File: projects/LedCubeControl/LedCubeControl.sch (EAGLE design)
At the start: 30 parts, among them IC1 74HC595N, IC2 74HC595N, IC3 74HC595N, T1 PN2222A, T2 PN2222A, T3 PN2222A, T4 PN2222A

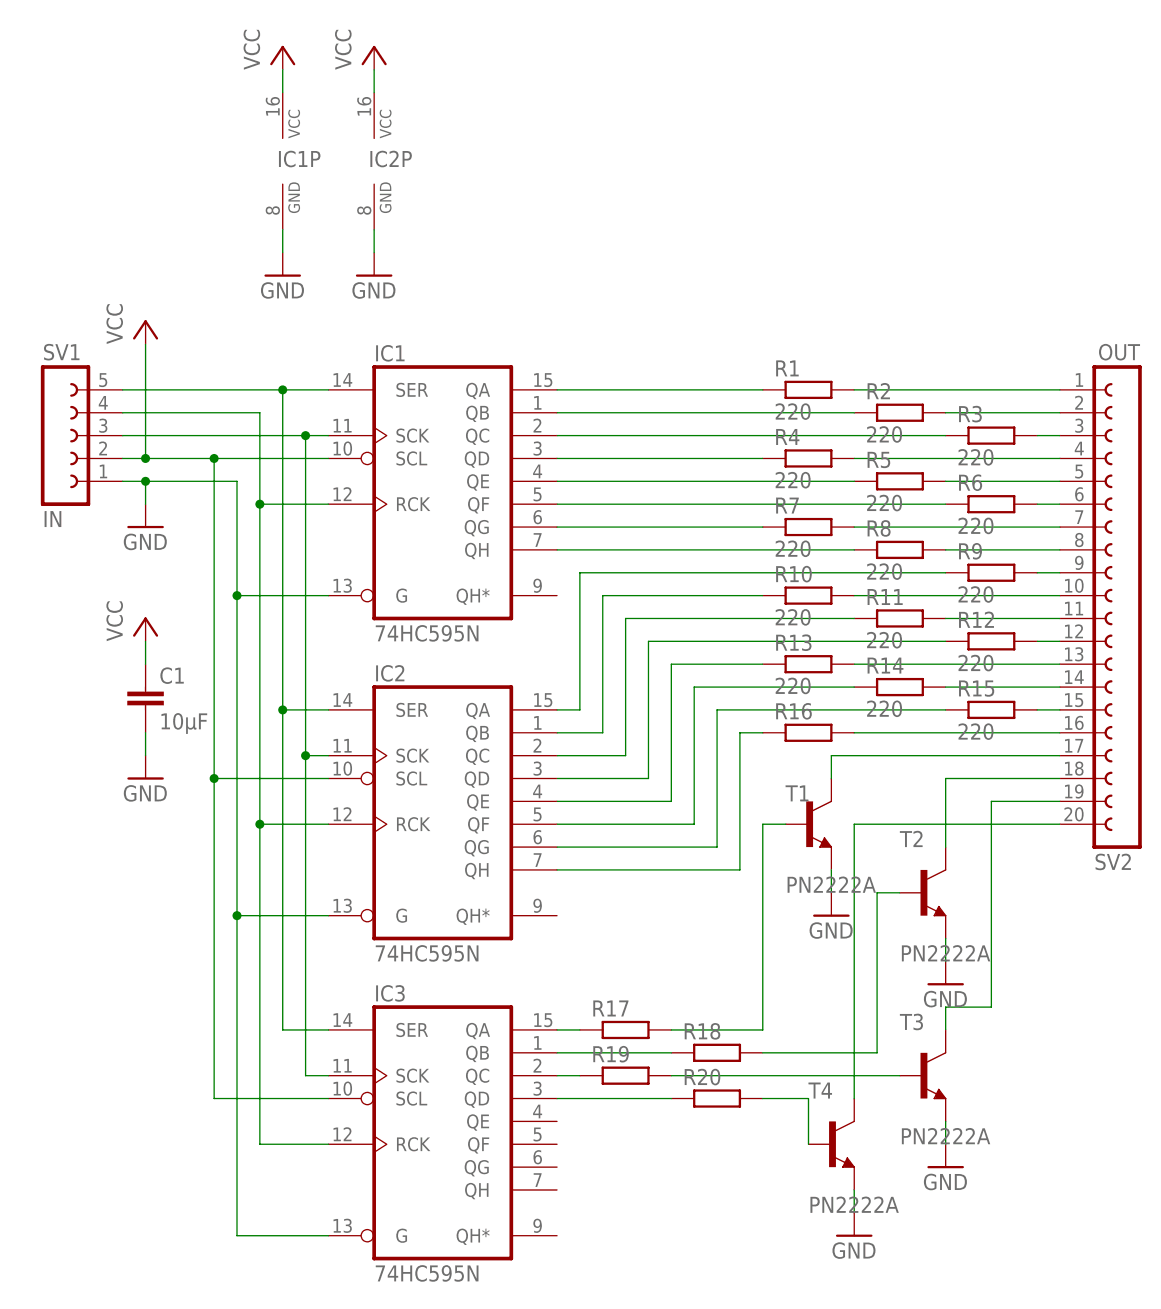
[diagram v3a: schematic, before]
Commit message: fix: mwrt and led control fixed
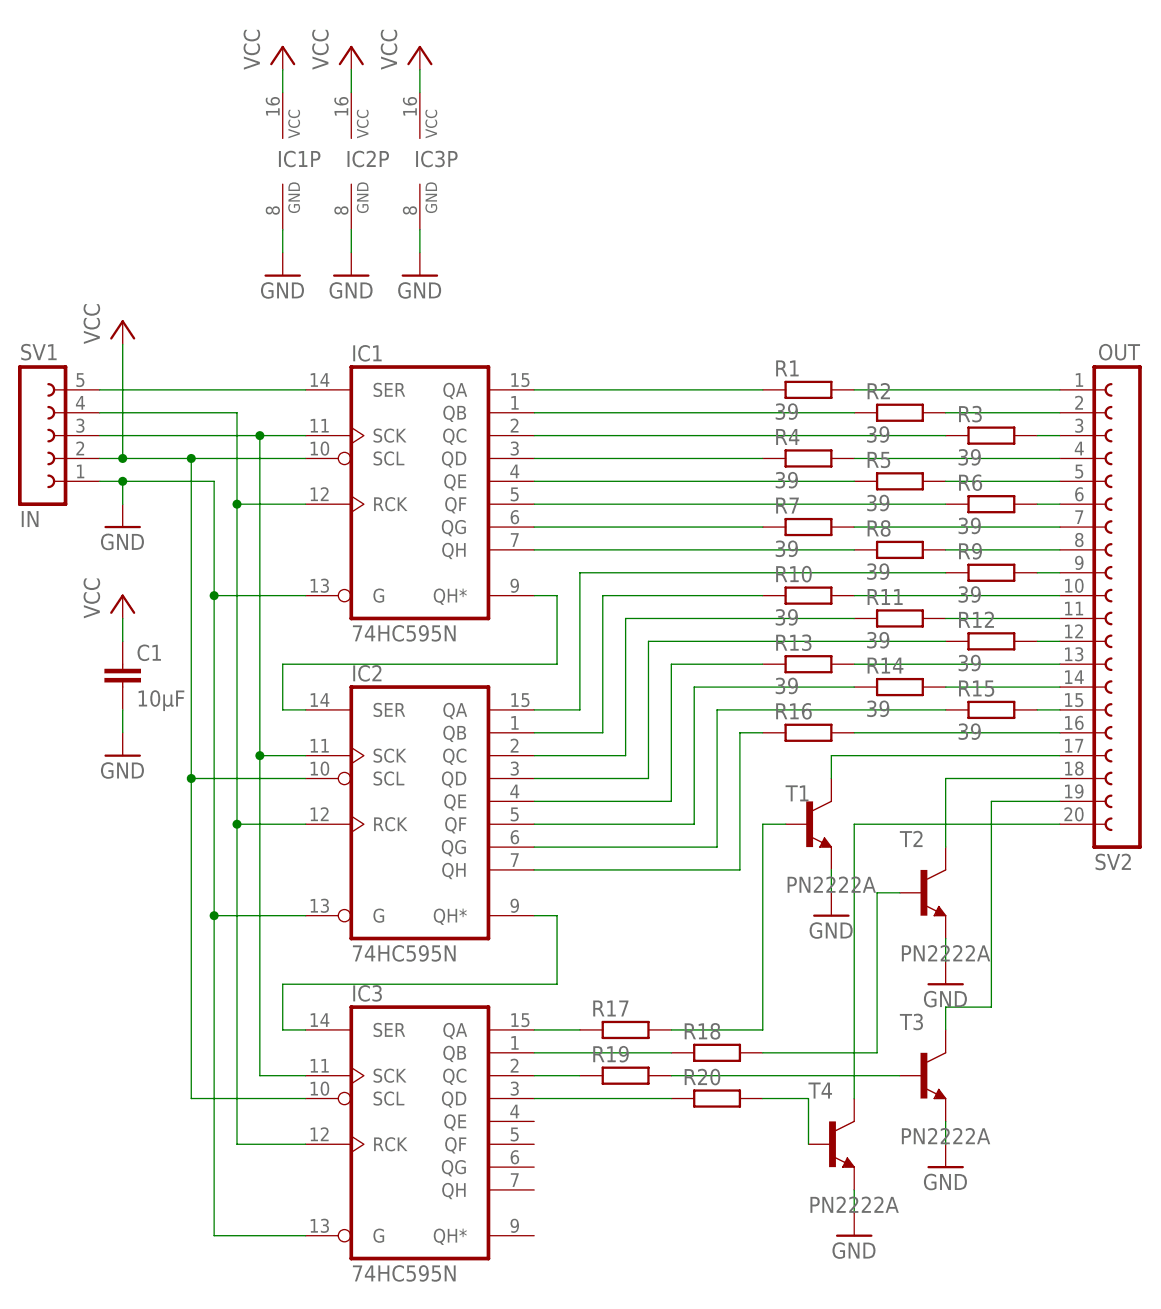
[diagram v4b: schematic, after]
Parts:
- R1, R10, R11, R12, R13, R14, R15, R16, R2, R3, R4, R5, R6, R7, R8, R9: value 220 -> 39
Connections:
- new net N$48: IC1A.SER, SV1.5
- new net N$49: IC2A.QH*, IC3A.SER
- net GND: now also IC3P.GND
- net N$2: now also IC1A.QH*; no longer IC1A.SER, IC3A.SER, SV1.5
- net VCC: now also IC3P.VCC
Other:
- moved on the sheet: C1, IC1, IC2, IC2P, IC3, SV1
